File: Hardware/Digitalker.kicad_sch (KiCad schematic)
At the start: 4 parts, among them U2 SN74LVC245APW, U3 SN74LVC245APW, U4 SN74LVC8T245, X1 ICSockets-40P

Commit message: digitalker work
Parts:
- added C1, C2, C3: 100nF, symbol Device:C
- added R1, R2: 10k, symbol Device:R_US
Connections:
- net at U3.1 (DIR): now also R2.1
- net GND: now reaches U3.10 (GND)
- net GND: now also U2.10 (GND), U2.19 (~{OE}), U3.19 (~{OE}), X1.20 (VSS), C1.1, C2.1
- net at U3.2 (A1): now also X1.33 (ADR8)
- net +3.3V: now reaches U3.20 (VCC)
- net +3.3V: now also U2.20 (VCC), C1.2, C2.2, R1.2, R2.2
- net at U2.1 (DIR): now also R1.1
- net at U2.2 (A1): now also X1.25 (ADR0_(LSB))
- net at U2.3 (A2): now also X1.26 (ADR1)
- net at U2.4 (A3): now also X1.27 (ADR2)
- net at U2.5 (A4): now also X1.28 (ADR3)
- net at U2.6 (A5): now also X1.29 (ADR4)
- net at U2.7 (A6): now also X1.30 (ADR5)
- net at U2.8 (A7): now also X1.31 (ADR6)
- net at U2.9 (A8): now also X1.32 (ADR7)
- net at U4.23 (V_{CCB}): no longer U4.24 (V_{CCB})
- net at X1.40 (VDD): now also C3.1
- now unconnected: U4.11 (GND), U4.12 (GND), U4.13 (GND)
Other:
- moved on the sheet: U2, X1

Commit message: bus connections to digitalker output level shifters
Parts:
- C1, C2: Voltage (none) -> 10V
- C3: Voltage (none) -> 25V
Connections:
- net GND: now also C3.2
- net +9V: now reaches C3.1, X1.40 (VDD)
- net at U3.3 (A2): now also X1.34 (ADR9)
- net at U3.4 (A3): now also X1.35 (ADR10)
- net at U3.5 (A4): now also X1.36 (ADR11)
- net at U3.6 (A5): now also X1.37 (ADR12)
- net at U3.7 (A6): now also X1.38 (ADR13_(MSB))
- net at U3.8 (A7): now also X1.5 (~{ROMEN})
- net at U3.9 (A8): now also X1.6 (INTR)

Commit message: finish digitalker
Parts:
- added C4, C5, C6, C7, C8, C9: 100nF, symbol Device:C
- added R3, R4, R5: 10k, symbol Device:R_US
- added U5, U6: SN74LVC8T245, symbol Logic_LevelTranslator:SN74LVC8T245
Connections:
- net +3.3V: now also U4.1 (V_{CCA}), C5.1, C6.1, C8.1, R3.2, R4.2, R5.2, U5.1 (V_{CCA}), U6.1 (V_{CCA})
- net GND: now also U4.10 (A8), U4.11 (GND), U4.12 (GND), U4.13 (GND), U4.14 (B8), U4.15 (B7), U4.16 (B6), U4.17 (B5), U4.22 (~{OE}), U4.7 (A5), U4.8 (A6), U4.9 (A7), C4.2, C5.2, C6.2, C7.2, C8.2, C9.2, U5.11 (GND), U5.12 (GND), U5.13 (GND), U5.22 (~{OE}), U6.11 (GND), U6.12 (GND), U6.13 (GND), U6.22 (~{OE})
- net ROM_ADDR7: now reaches U2.11 (B8)
- net ROM_ADDR6: now reaches U2.12 (B7)
- net ROM_ADDR5: now reaches U2.13 (B6)
- net ROM_ADDR4: now reaches U2.14 (B5)
- net ROM_ADDR3: now reaches U2.15 (B4)
- net ROM_ADDR2: now reaches U2.16 (B3)
- net ROM_ADDR1: now reaches U2.17 (B2)
- net ROM_ADDR0: now reaches U2.18 (B1)
- net DIGI_ROM_ADDR0: now reaches U2.2 (A1), X1.25 (ADR0_(LSB))
- net DIGI_ROM_ADDR1: now reaches U2.3 (A2), X1.26 (ADR1)
- net DIGI_ROM_ADDR2: now reaches U2.4 (A3), X1.27 (ADR2)
- net DIGI_ROM_ADDR3: now reaches U2.5 (A4), X1.28 (ADR3)
- net DIGI_ROM_ADDR4: now reaches U2.6 (A5), X1.29 (ADR4)
- net DIGI_ROM_ADDR5: now reaches U2.7 (A6), X1.30 (ADR5)
- net DIGI_ROM_ADDR6: now reaches U2.8 (A7), X1.31 (ADR6)
- net DIGI_ROM_ADDR7: now reaches U2.9 (A8), X1.32 (ADR7)
- net DIGI_CMS: now reaches U4.18 (B4)
- net DIGI_CMS: now also X1.7 (CMS)
- net DIGI_~{WR}: now reaches U4.19 (B3)
- net DIGI_~{WR}: now also X1.4 (~{WR})
- net at U4.2 (DIR): now also R3.1
- net DIGI_~{CS}: now reaches U4.20 (B2)
- net DIGI_~{CS}: now also X1.3 (~{CS})
- net DIGI_CLK_4MHZ: now reaches U4.21 (B1)
- net DIGI_CLK_4MHZ: now also X1.1 (OSC_IN)
- net +5V: now reaches U4.23 (V_{CCB})
- net +5V: now also U4.24 (V_{CCB}), C4.1, C7.1, C9.1, U5.23 (V_{CCB}), U5.24 (V_{CCB}), U6.23 (V_{CCB}), U6.24 (V_{CCB})
- net DIGITALKER_CLK_4MHZ: now reaches U4.3 (A1)
- net ~{DIGITALKER_CS}: now reaches U4.4 (A2)
- net ~{DIGITALKER_WR}: now reaches U4.5 (A3)
- net DIGITALKER_CMS: now reaches U4.6 (A4)
- net INTR: now reaches U3.11 (B8)
- net ~{ROMEN}: now reaches U3.12 (B7)
- net ROM_ADDR13: now reaches U3.13 (B6)
- net ROM_ADDR12: now reaches U3.14 (B5)
- net ROM_ADDR11: now reaches U3.15 (B4)
- net ROM_ADDR10: now reaches U3.16 (B3)
- net ROM_ADDR9: now reaches U3.17 (B2)
- net ROM_ADDR8: now reaches U3.18 (B1)
- net DIGI_ROM_ADDR8: now reaches U3.2 (A1), X1.33 (ADR8)
- net DIGI_ROM_ADDR9: now reaches U3.3 (A2), X1.34 (ADR9)
- net DIGI_ROM_ADDR10: now reaches U3.4 (A3), X1.35 (ADR10)
- net DIGI_ROM_ADDR11: now reaches U3.5 (A4), X1.36 (ADR11)
- net DIGI_ROM_ADDR12: now reaches U3.6 (A5), X1.37 (ADR12)
- net DIGI_ROM_ADDR13: now reaches U3.7 (A6), X1.38 (ADR13_(MSB))
- net DIGI_~{ROMEN}: now reaches U3.8 (A7), X1.5 (~{ROMEN})
- net DIGI_INTR: now reaches U3.9 (A8), X1.6 (INTR)
- net DIGI_SW6: now reaches X1.10 (SW6)
- net DIGI_SW6: now also U5.16 (B6)
- net DIGI_SW5: now reaches X1.11 (SW5)
- net DIGI_SW5: now also U5.17 (B5)
- net DIGI_SW4: now reaches X1.12 (SW4)
- net DIGI_SW4: now also U5.18 (B4)
- net DIGI_SW3: now reaches X1.13 (SW3)
- net DIGI_SW3: now also U5.19 (B3)
- net DIGI_SW2: now reaches X1.14 (SW2)
- net DIGI_SW2: now also U5.20 (B2)
- net DIGI_SW1: now reaches X1.15 (SW1_(LSB))
- net DIGI_SW1: now also U5.21 (B1)
- net DIGI_RDATA0: now reaches X1.16 (RDATA0_(LSB))
- net DIGI_RDATA0: now also U6.21 (B1)
- net DIGI_RDATA1: now reaches X1.17 (RDATA1)
- net DIGI_RDATA1: now also U6.20 (B2)
- net DIGI_RDATA2: now reaches X1.18 (RDATA2)
- net DIGI_RDATA2: now also U6.19 (B3)
- net DIGI_RDATA3: now reaches X1.19 (RDATA3)
- net DIGI_RDATA3: now also U6.18 (B4)
- net DIGI_RDATA4: now reaches X1.21 (RDATA4)
- net DIGI_RDATA4: now also U6.17 (B5)
- net DIGI_RDATA5: now reaches X1.22 (RDATA5)
- net DIGI_RDATA5: now also U6.16 (B6)
- net DIGI_RDATA6: now reaches X1.23 (RDATA6)
- net DIGI_RDATA6: now also U6.15 (B7)
- net DIGI_RDATA7: now reaches X1.24 (RDATA7)
- net DIGI_RDATA7: now also U6.14 (B8)
- net DIGI_SW8: now reaches X1.8 (SW8_(MSB))
- net DIGI_SW8: now also U5.14 (B8)
- net DIGI_SW7: now reaches X1.9 (SW7)
- net DIGI_SW7: now also U5.15 (B7)
- new net: R4.1, U5.2 (DIR)
- new net: R5.1, U6.2 (DIR)
- new net RDATA0: U6.3 (A1)
- new net RDATA1: U6.4 (A2)
- new net RDATA2: U6.5 (A3)
- new net RDATA3: U6.6 (A4)
- new net RDATA4: U6.7 (A5)
- new net RDATA5: U6.8 (A6)
- new net RDATA6: U6.9 (A7)
- new net RDATA7: U6.10 (A8)
- new net SW1: U5.3 (A1)
- new net SW2: U5.4 (A2)
- new net SW3: U5.5 (A3)
- new net SW4: U5.6 (A4)
- new net SW5: U5.7 (A5)
- new net SW6: U5.8 (A6)
- new net SW7: U5.9 (A7)
- new net SW8: U5.10 (A8)
- no-connect marks 0 -> 1
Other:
- moved on the sheet: C1, C2, C3, R1, R2, U2, U3, U4, X1

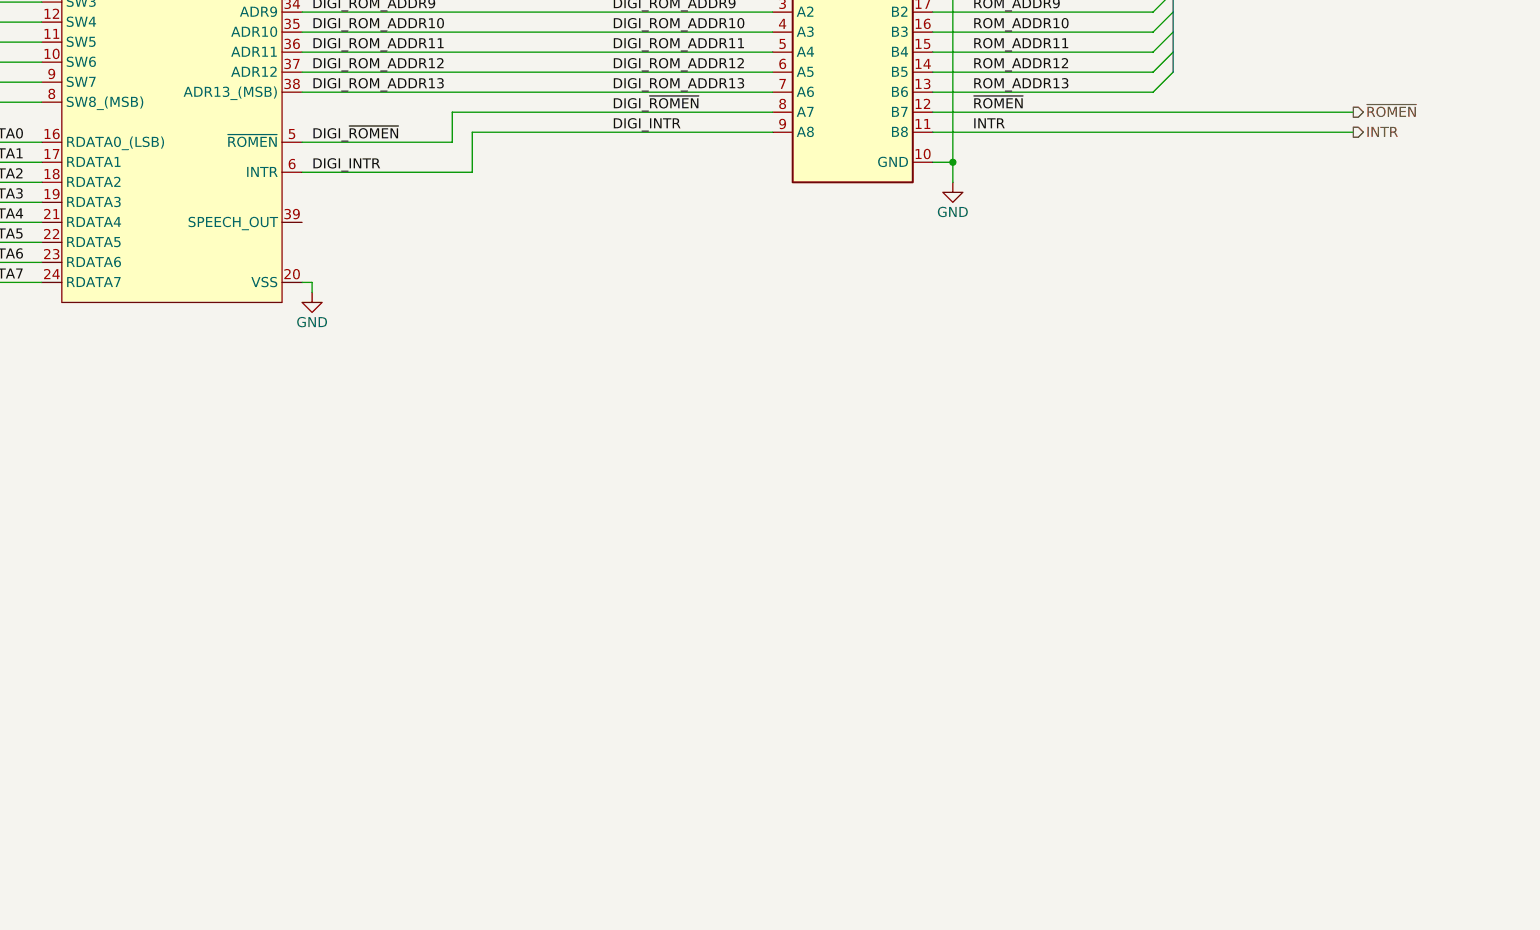
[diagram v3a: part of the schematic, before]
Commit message: implement speech filter
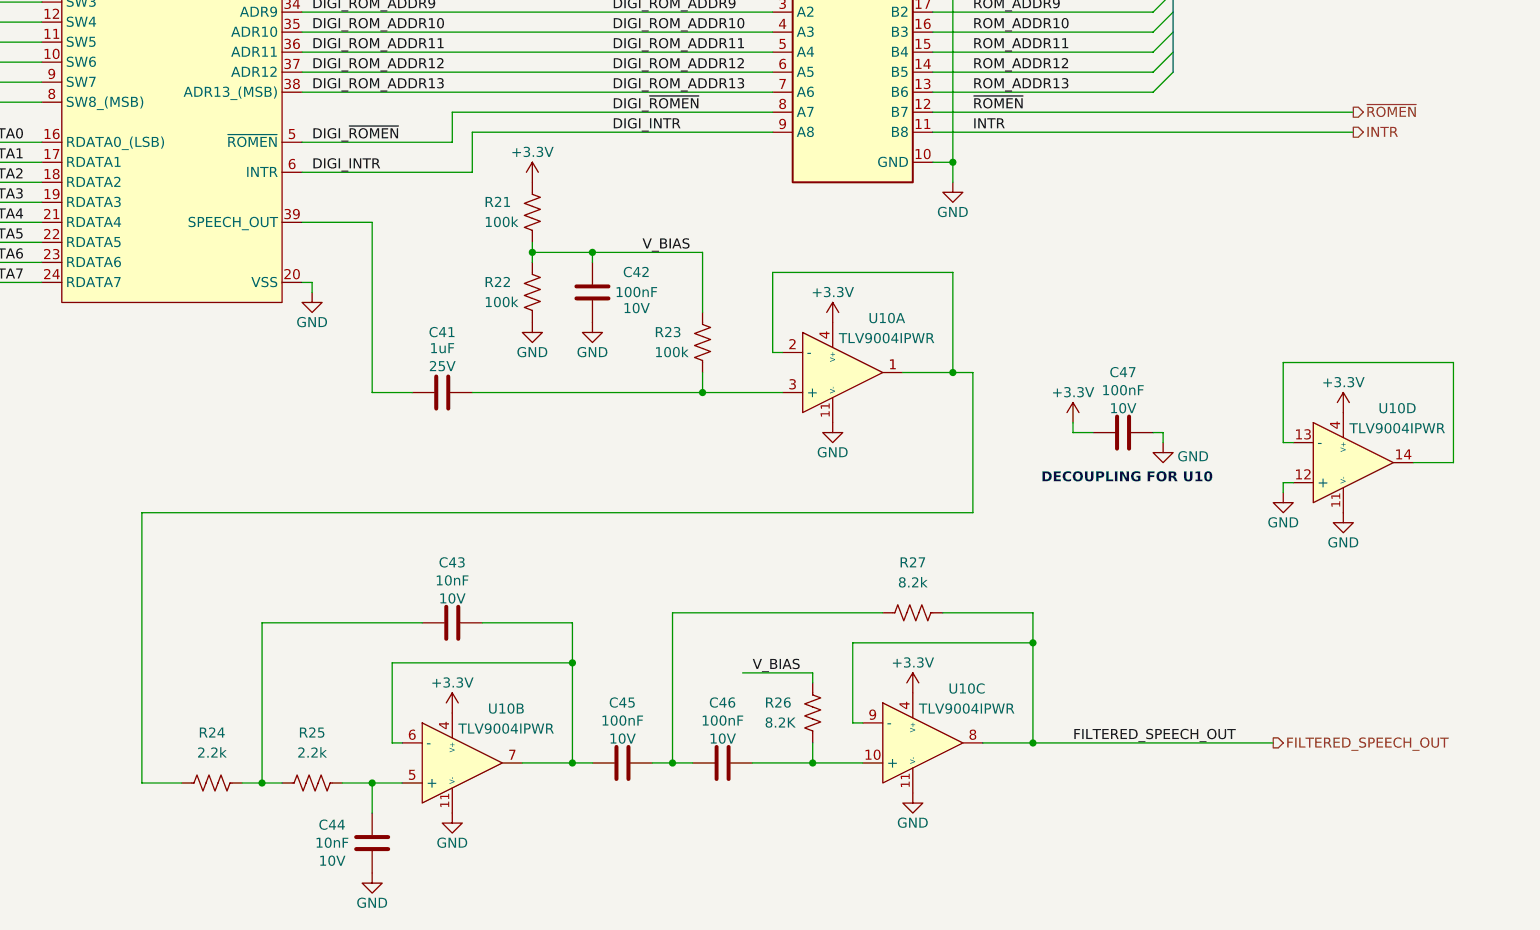
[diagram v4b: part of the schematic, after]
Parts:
- added C41: 1uF, symbol Device:C
- added C42, C45, C46, C47: 100nF, symbol Device:C
- added C43, C44: 10nF, symbol Device:C
- added R21, R22, R23: 100k, symbol Device:R_US
- added R24, R25: 2.2k, symbol Device:R_US
- added R26: 8.2K, symbol Device:R_US
- added R27: 8.2k, symbol Device:R_US
- added U10: TLV9004IPWR, symbol Digichiver:TLV9004
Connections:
- net +3.3V: now also C47.2, R21.2, U10.4 (V+), U10.4 (V+), U10.4 (V+), U10.4 (V+)
- net GND: now also C42.2, C44.2, C47.1, R22.1, U10.11 (V-), U10.11 (V-), U10.11 (V-), U10.11 (V-), U10.12 (+)
- net at X1.39 (SPEECH_OUT): now also C41.2
- new net: C44.1, R25.1, U10.5 (+)
- new net: C43.1, C45.2, U10.6 (-), U10.7
- new net: C41.1, R23.1, U10.3 (+)
- new net: R24.2, U10.1, U10.2 (-)
- new net: C46.1, R26.1, U10.10 (+)
- new net: C43.2, R24.1, R25.2
- new net: C45.1, C46.2, R27.2
- new net: U10.13 (-), U10.14
- new net FILTERED_SPEECH_OUT: R27.1, U10.8, U10.9 (-)
- new net V_BIAS: C42.1, R21.1, R22.2, R23.2, R26.2
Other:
- note added: "DECOUPLING FOR U10"

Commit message: file renaming
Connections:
- net FILTERED_SPEECH_OUT renamed FILTERED_SPEECH

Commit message: footprint assignment
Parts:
- C1, C2, C4, C42, C45, C46, C47, C5, C6, C7, C8, C9: footprint (none) -> Capacitor_SMD:C_0402_1005Metric; MPN (none) -> GRM155R71A104KA01D
- C3: footprint (none) -> Capacitor_SMD:C_0402_1005Metric; MPN (none) -> CC0402KRX7R8BB104
- C41: footprint (none) -> Capacitor_SMD:C_0402_1005Metric; MPN (none) -> CL05A105KA5NQNC
- C43, C44: footprint (none) -> Capacitor_SMD:C_0402_1005Metric; MPN (none) -> CL05B103KB5NNNC
- U10: footprint (none) -> Package_SO:TSSOP-14_4.4x5mm_P0.65mm; MPN (none) -> TLV9004IPW
- U2, U3: value SN74LVC245APW -> SN74LVC245A; MPN (none) -> SN74LVC245APW
- U4, U5, U6: footprint (none) -> Package_SO:TSSOP-24_4.4x6.5mm_P0.5mm; MPN (none) -> SN74LVC8T245PW
- X1: MPN (none) -> ICSockets-40P

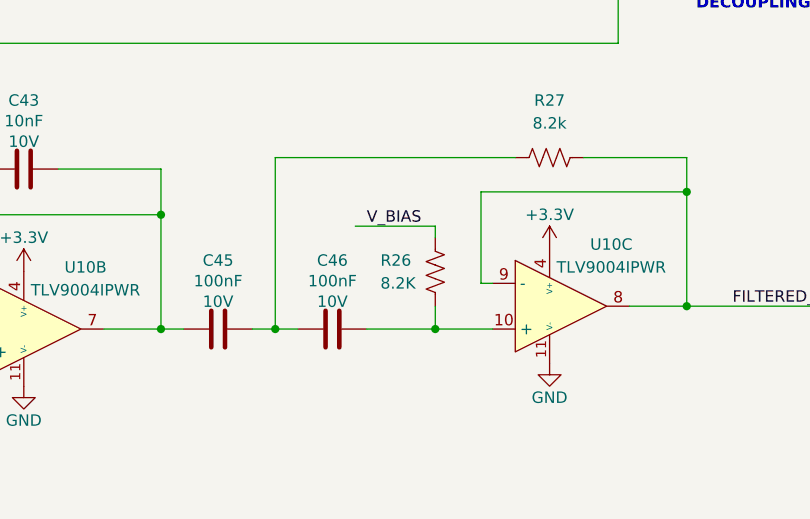
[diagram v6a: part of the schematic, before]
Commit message: link footprints to symbols
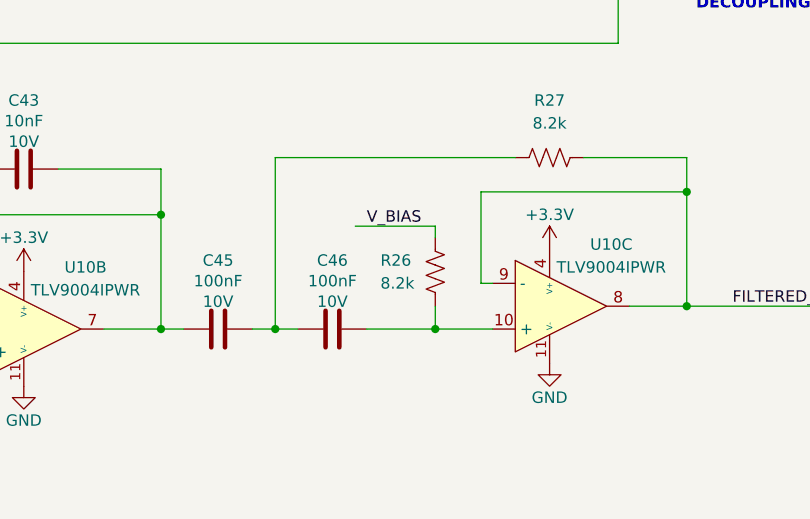
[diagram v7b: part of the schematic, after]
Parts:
- R1, R2, R3, R4, R5: footprint (none) -> Resistor_SMD:R_0402_1005Metric; MPN (none) -> RC0402FR-0710KL
- R21, R22, R23: footprint (none) -> Resistor_SMD:R_0402_1005Metric; MPN (none) -> RC0402FR-07100KL
- R24, R25: footprint (none) -> Resistor_SMD:R_0402_1005Metric; MPN (none) -> RC0402JR-072K2L
- R26: value 8.2K -> 8.2k; footprint (none) -> Resistor_SMD:R_0402_1005Metric; MPN (none) -> RT0402BRD078K2L
- R27: footprint (none) -> Resistor_SMD:R_0402_1005Metric; MPN (none) -> RT0402BRD078K2L
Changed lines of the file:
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@@
 			)
 		)
-		(property "Footprint" ""
+		(property "Footprint" "Resistor_SMD:R_0402_1005Metric"
 			(at 282.194 163.576 90)
 			(hide yes)
@@
 			)
 		)
-		(property "Datasheet" ""
+		(property "Datasheet" "https://yageogroup.com/content/datasheet/asset/file/PYU-RC_GROUP_51_ROHS_L"
 			(at 283.21 163.83 0)
 			(hide yes)
@@
 			)
 		)
+		(property "MPN" "RC0402FR-07100KL"
+			(at 283.21 163.83 0)
+			(hide yes)
+			(show_name no)
+			(do_not_autoplace no)
+			(effects
+				(font
+					(size 1.27 1.27)
+				)
+			)
+		)
 		(pin "1"
 		)
@@
 			)
 		)
-		(property "Footprint" ""
+		(property "Footprint" "Resistor_SMD:R_0402_1005Metric"
 			(at 280.924 111.506 90)
 			(hide yes)
@@
 			)
 		)
-		(property "Datasheet" ""
+		(property "Datasheet" "https://yageogroup.com/content/datasheet/asset/file/PYU-RC_GROUP_51_ROHS_L"
 			(at 281.94 111.76 0)
 			(hide yes)
@@
 			)
 		)
+		(property "MPN" "RC0402FR-0710KL"
+			(at 281.94 111.76 0)
+			(hide yes)
+			(show_name no)
+			(do_not_autoplace no)
+			(effects
+				(font
+					(size 1.27 1.27)
+				)
+			)
+		)
 		(pin "1"
 		)
@@
 			)
 		)
-		(property "Footprint" ""
+		(property "Footprint" "Resistor_SMD:R_0402_1005Metric"
 			(at 233.426 220.726 90)
 			(hide yes)
@@
 			)
 		)
-		(property "Datasheet" ""
+		(property "Datasheet" "https://yageogroup.com/content/datasheet/asset/file/PYU-RC_GROUP_51_ROHS_L"
 			(at 233.68 219.71 0)
 			(hide yes)
@@
 			)
 		)
+		(property "MPN" "RC0402JR-072K2L"
+			(at 233.68 219.71 90)
+			(hide yes)
+			(show_name no)
+			(do_not_autoplace no)
+			(effects
+				(font
+					(size 1.27 1.27)
+				)
+			)
+		)
 		(pin "1"
 		)
@@
 			)
 		)
-		(property "Footprint" ""
+		(property "Footprint" "Resistor_SMD:R_0402_1005Metric"
 			(at 220.726 220.726 90)
 			(hide yes)
@@
 			)
 		)
-		(property "Datasheet" ""
+		(property "Datasheet" "https://yageogroup.com/content/datasheet/asset/file/PYU-RC_GROUP_51_ROHS_L"
 			(at 220.98 219.71 0)
 			(hide yes)
@@
 			)
 		)
+		(property "MPN" "RC0402JR-072K2L"
+			(at 220.98 219.71 90)
+			(hide yes)
+			(show_name no)
+			(do_not_autoplace no)
+			(effects
+				(font
+					(size 1.27 1.27)
+				)
+			)
+		)
 		(pin "1"
 		)
@@
 			)
 		)
-		(property "Footprint" ""
+		(property "Footprint" "Resistor_SMD:R_0402_1005Metric"
 			(at 280.924 61.976 90)
 			(hide yes)
@@
 			)
 		)
-		(property "Datasheet" ""
+		(property "Datasheet" "https://yageogroup.com/content/datasheet/asset/file/PYU-RC_GROUP_51_ROHS_L"
 			(at 281.94 62.23 0)
 			(hide yes)
@@
 			)
 		)
+		(property "MPN" "RC0402FR-0710KL"
+			(at 281.94 62.23 0)
+			(hide yes)
+			(show_name no)
+			(do_not_autoplace no)
+			(effects
+				(font
+					(size 1.27 1.27)
+				)
+			)
+		)
 		(pin "1"
 		)
@@
 			)
 		)
-		(property "Footprint" ""
+		(property "Footprint" "Resistor_SMD:R_0402_1005Metric"
 			(at 260.604 147.066 90)
 			(hide yes)
@@
 			)
 		)
-		(property "Datasheet" ""
+		(property "Datasheet" "https://yageogroup.com/content/datasheet/asset/file/PYU-RC_GROUP_51_ROHS_L"
 			(at 261.62 147.32 0)
 			(hide yes)
@@
 			)
 		)
+		(property "MPN" "RC0402FR-07100KL"
+			(at 261.62 147.32 0)
+			(hide yes)
+			(show_name no)
+			(do_not_autoplace no)
+			(effects
+				(font
+					(size 1.27 1.27)
+				)
+			)
+		)
 		(pin "1"
 		)
@@
 			)
 		)
-		(property "Footprint" ""
+		(property "Footprint" "Resistor_SMD:R_0402_1005Metric"
 			(at 260.604 157.226 90)
 			(hide yes)
@@
 			)
 		)
-		(property "Datasheet" ""
+		(property "Datasheet" "https://yageogroup.com/content/datasheet/asset/file/PYU-RC_GROUP_51_ROHS_L"
 			(at 261.62 157.48 0)
 			(hide yes)
@@
 			)
 		)
+		(property "MPN" "RC0402FR-07100KL"
+			(at 261.62 157.48 0)
+			(hide yes)
+			(show_name no)
+			(do_not_autoplace no)
+			(effects
+				(font
+					(size 1.27 1.27)
+				)
+			)
+		)
 		(pin "1"
 		)
@@
 			)
 		)
-		(property "Footprint" ""
+		(property "Footprint" "Resistor_SMD:R_0402_1005Metric"
 			(at 97.536 194.056 90)
 			(hide yes)
@@
 			)
 		)
-		(property "Datasheet" ""
+		(property "Datasheet" "https://yageogroup.com/content/datasheet/asset/file/PYU-RC_GROUP_51_ROHS_L"
 			(at 97.79 193.04 0)
 			(hide yes)
@@
 			)
 		)
+		(property "MPN" "RC0402FR-0710KL"
+			(at 97.79 193.04 90)
+			(hide yes)
+			(show_name no)
+			(do_not_autoplace no)
+			(effects
+				(font
+					(size 1.27 1.27)
+				)
+			)
+		)
 		(pin "1"
 		)
@@
 			)
 		)
-		(property "Footprint" ""
+		(property "Footprint" "Resistor_SMD:R_0402_1005Metric"
 			(at 97.536 128.016 90)
 			(hide yes)
@@
 			)
 		)
-		(property "Datasheet" ""
+		(property "Datasheet" "https://yageogroup.com/content/datasheet/asset/file/PYU-RC_GROUP_51_ROHS_L"
 			(at 97.79 127 0)
 			(hide yes)
@@
 			)
 		)
+		(property "MPN" "RC0402FR-0710KL"
+			(at 97.79 127 90)
+			(hide yes)
+			(show_name no)
+			(do_not_autoplace no)
+			(effects
+				(font
+					(size 1.27 1.27)
+				)
+			)
+		)
 		(pin "1"
 		)
@@
 			)
 		)
-		(property "Footprint" ""
+		(property "Footprint" "Resistor_SMD:R_0402_1005Metric"
 			(at 309.626 199.136 90)
 			(hide yes)
@@
 			)
 		)
-		(property "Datasheet" ""
+		(property "Datasheet" "https://yageogroup.com/content/datasheet/asset/file/PYU-RT_1-TO-0-01_ROHS_L"
 			(at 309.88 198.12 0)
 			(hide yes)
@@
 			)
 		)
+		(property "MPN" "RT0402BRD078K2L"
+			(at 309.88 198.12 90)
+			(hide yes)
+			(show_name no)
+			(do_not_autoplace no)
+			(effects
+				(font
+					(size 1.27 1.27)
+				)
+			)
+		)
 		(pin "1"
 		)
@@
 			)
 		)
-		(property "Value" "8.2K"
+		(property "Value" "8.2k"
 			(at 291.084 212.09 0)
 			(show_name no)
@@
 			)
 		)
-		(property "Footprint" ""
+		(property "Footprint" "Resistor_SMD:R_0402_1005Metric"
 			(at 296.164 210.566 90)
 			(hide yes)
@@
 			)
 		)
-		(property "Datasheet" ""
+		(property "Datasheet" "https://yageogroup.com/content/datasheet/asset/file/PYU-RT_1-TO-0-01_ROHS_L"
 			(at 297.18 210.82 0)
 			(hide yes)
@@
 			)
 		)
+		(property "MPN" "RT0402BRD078K2L"
+			(at 297.18 210.82 0)
+			(hide yes)
+			(show_name no)
+			(do_not_autoplace no)
+			(effects
+				(font
+					(size 1.27 1.27)
+				)
+			)
+		)
 		(pin "1"
 		)
@@
 			)
 		)
-		(property "Footprint" ""
+		(property "Footprint" "Resistor_SMD:R_0402_1005Metric"
 			(at 97.536 61.976 90)
 			(hide yes)
@@
 			)
 		)
-		(property "Datasheet" ""
+		(property "Datasheet" "https://yageogroup.com/content/datasheet/asset/file/PYU-RC_GROUP_51_ROHS_L"
 			(at 97.79 60.96 0)
 			(hide yes)
@@
 			(at 97.79 60.96 90)
 			(hide yes)
+			(show_name no)
+			(do_not_autoplace no)
+			(effects
+				(font
+					(size 1.27 1.27)
+				)
+			)
+		)
+		(property "MPN" "RC0402FR-0710KL"
+			(at 97.79 60.96 90)
+			(hide yes)
